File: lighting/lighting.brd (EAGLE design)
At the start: 22.5 x 12.5 mm, 6 parts, among them J1 22-05-3021

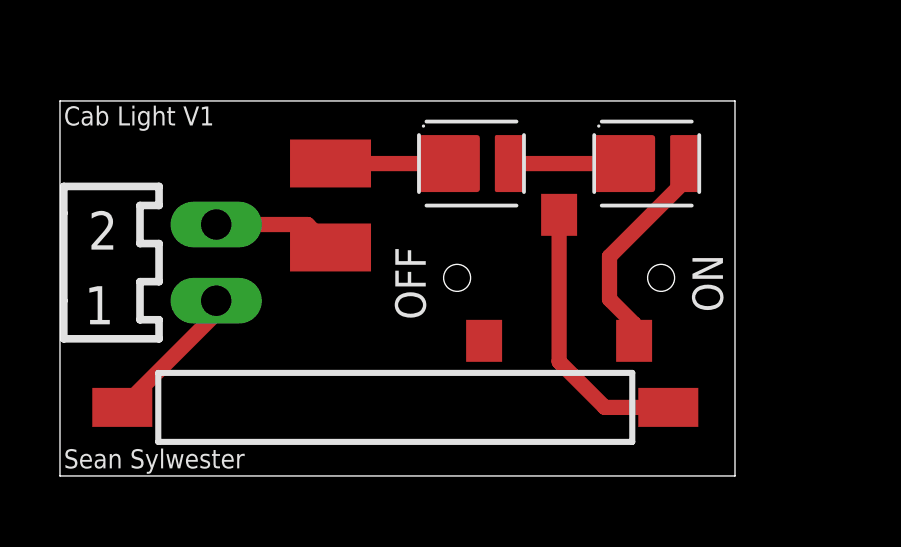
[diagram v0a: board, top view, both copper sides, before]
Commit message: fixed LED direction; GND plane
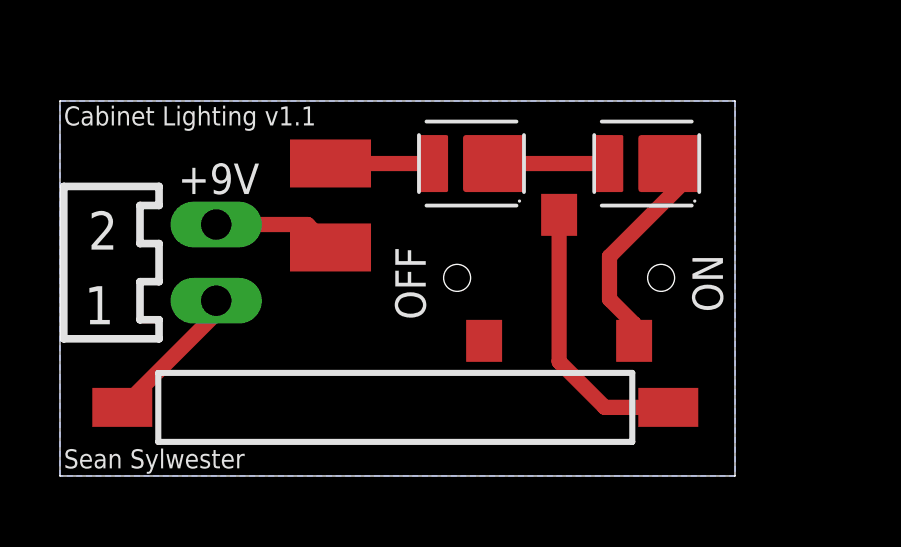
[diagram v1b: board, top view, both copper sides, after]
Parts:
- turned D1 to 180 degrees
- turned D2 to 180 degrees
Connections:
- net N$1 renamed GND
- net N$6 renamed VCC
- net N$3: now also D2.-; no longer D2.+
- net N$4: now also D1.-, D2.+; no longer D1.+, D2.-
- net N$5: now also D1.+; no longer D1.-
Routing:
- net N$5: track 3.97 -> 3.44 mm
- added copper zone on layer 16, net GND
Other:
- board text added: "+9V"
- board text added: "Cabinet Lighting v1.1"
- board text removed: "Cab Light V1"
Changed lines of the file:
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@@
 <setting verticaltext="up"/>
 </settings>
-<grid distance="5" unitdist="mil" unit="mil" style="lines" multiple="1" display="no" altdistance="5" altunitdist="mil" altunit="mil"/>
+<grid distance="1" unitdist="mil" unit="mil" style="lines" multiple="1" display="no" altdistance="5" altunitdist="mil" altunit="mil"/>
 <layers>
 <layer number="1" name="Top" color="4" fill="1" visible="yes" active="yes"/>
@@
 <text x="22.098" y="5.461" size="1.016" layer="21" rot="R90">ON</text>
 <text x="12.192" y="5.207" size="1.016" layer="21" rot="R90">OFF</text>
-<text x="0.127" y="11.684" size="0.635" layer="21">Cab Light V1</text>
+<text x="0.127" y="11.684" size="0.635" layer="21">Cabinet Lighting v1.1</text>
 <text x="0.127" y="0.254" size="0.635" layer="21">Sean Sylwester</text>
+<text x="3.937" y="9.398" size="1.016" layer="21">+9V</text>
 </plain>
 <attributes>
@@
 </class>
 </classes>
-<designrules name="default">
+<designrules name="default *">
 <description language="de">&lt;b&gt;EAGLE Design Rules&lt;/b&gt;
 &lt;p&gt;
@@
 <param name="mdViaViaSameLayer" value="6mil"/>
 <param name="mnLayersViaInSmd" value="2"/>
-<param name="mdCopperDimension" value="40mil"/>
+<param name="mdCopperDimension" value="8mil"/>
 <param name="mdDrill" value="6mil"/>
 <param name="mdSmdStop" value="0mil"/>
@@
 <attribute name="VALUE" x="17.526" y="2.921" size="1.27" layer="27" rot="R180"/>
 </element>
-<element name="D1" library="my_lib" package="LUXEON2835C" value="LUXEON2835C" x="13.716" y="10.414" smashed="yes"/>
-<element name="D2" library="my_lib" package="LUXEON2835C" value="LUXEON2835C" x="19.558" y="10.414" smashed="yes"/>
+<element name="D1" library="my_lib" package="LUXEON2835C" value="LUXEON2835C" x="13.716" y="10.414" smashed="yes" rot="R180"/>
+<element name="D2" library="my_lib" package="LUXEON2835C" value="LUXEON2835C" x="19.558" y="10.414" smashed="yes" rot="R180"/>
 <element name="S2" library="my_lib" package="CL-SB-12B-01T" value="CL-SB-12B-01T" x="16.637" y="6.604" smashed="yes">
 <attribute name="VALUE" x="13.422" y="2.274" size="1.27" layer="27"/>
@@
 </elements>
 <signals>
-<signal name="N$1">
+<signal name="GND">
 <contactref element="S1" pad="2"/>
 <contactref element="J1" pad="1"/>
 <wire x1="2.076" y1="2.286" x2="5.207" y2="5.417" width="0.508" layer="1"/>
 <wire x1="5.207" y1="5.417" x2="5.207" y2="5.842" width="0.508" layer="1"/>
+<polygon width="0.127" layer="16" spacing="0.254" orphans="yes" thermals="no">
+<vertex x="0" y="12.4968"/>
+<vertex x="22.5044" y="12.4968"/>
+<vertex x="22.5044" y="0"/>
+<vertex x="0" y="0"/>
+</polygon>
 </signal>
 <signal name="N$3">
-<contactref element="D2" pad="+"/>
+<contactref element="D2" pad="-"/>
 <contactref element="S2" pad="P$3"/>
 <wire x1="18.317" y1="5.89155" x2="18.317" y2="7.31645" width="0.508" layer="1"/>
 <wire x1="19.137" y1="4.504" x2="19.137" y2="5.07155" width="0.508" layer="1"/>
 <wire x1="19.137" y1="5.07155" x2="18.317" y2="5.89155" width="0.508" layer="1"/>
-<wire x1="20.823" y1="9.82245" x2="20.823" y2="10.414" width="0.508" layer="1"/>
+<wire x1="20.823" y1="9.82245" x2="20.293" y2="10.414" width="0.508" layer="1"/>
 <wire x1="18.317" y1="7.31645" x2="20.823" y2="9.82245" width="0.508" layer="1"/>
 </signal>
 <signal name="N$5">
 <contactref element="R1" pad="2"/>
-<contactref element="D1" pad="-"/>
-<wire x1="12.981" y1="10.414" x2="9.02" y2="10.414" width="0.508" layer="1"/>
+<contactref element="D1" pad="+"/>
+<wire x1="12.451" y1="10.414" x2="9.02" y2="10.414" width="0.508" layer="1"/>
 <wire x1="9.02" y1="10.414" x2="9.017" y2="10.417" width="0.254" layer="1"/>
 </signal>
-<signal name="N$6">
+<signal name="VCC">
 <contactref element="R1" pad="1"/>
 <contactref element="J1" pad="2"/>
@@
 </signal>
 <signal name="N$4">
-<contactref element="D1" pad="+"/>
-<contactref element="D2" pad="-"/>
-<wire x1="14.981" y1="10.414" x2="18.823" y2="10.414" width="0.508" layer="1"/>
+<contactref element="D1" pad="-"/>
+<contactref element="D2" pad="+"/>
+<wire x1="14.451" y1="10.414" x2="18.293" y2="10.414" width="0.508" layer="1"/>
 </signal>
 <signal name="N$2">
@@
 <mfgpreviewcolor name="substratecolor" color="0xFF786E46"/>
 </mfgpreviewcolors>
+<errors>
+</errors>
 </board>
 </drawing>

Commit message: added mounting holes
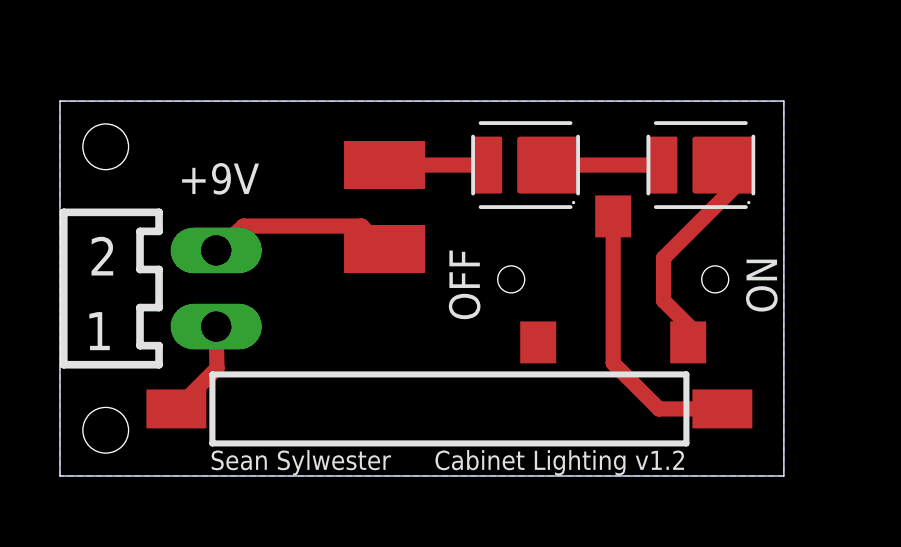
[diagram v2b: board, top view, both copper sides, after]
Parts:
- moved D1 1.80 mm to (15.5, 10.4)
- moved D2 1.80 mm to (21.4, 10.4)
- moved R1 1.80 mm to (10.8, 8.97)
- moved S1 1.80 mm to (13.0, 2.24)
- moved S2 1.80 mm to (18.4, 6.55)
- moved J1 0.86 mm to (5.21, 6.25)
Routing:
- net VCC: track 4.13 -> 6.24 mm
- net GND: track 4.85 -> 3.30 mm
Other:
- board size 22.5 x 12.5 mm -> 24.1 x 12.5 mm
- board text added: "Cabinet Lighting v1.2"
- board text removed: "Cabinet Lighting v1.1"
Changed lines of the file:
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@@
 <layer number="43" name="vRestrict" color="2" fill="10" visible="yes" active="yes"/>
 <layer number="44" name="Drills" color="7" fill="1" visible="no" active="yes"/>
-<layer number="45" name="Holes" color="7" fill="1" visible="no" active="yes"/>
+<layer number="45" name="Holes" color="7" fill="1" visible="yes" active="yes"/>
 <layer number="46" name="Milling" color="3" fill="1" visible="no" active="yes"/>
 <layer number="47" name="Measures" color="7" fill="1" visible="no" active="yes"/>
@@
 <board>
 <plain>
-<wire x1="0" y1="0" x2="22.5" y2="0" width="0" layer="20"/>
-<wire x1="22.5" y1="0" x2="22.5" y2="12.5" width="0" layer="20"/>
-<wire x1="22.5" y1="12.5" x2="0" y2="12.5" width="0" layer="20"/>
-<wire x1="0" y1="12.5" x2="0" y2="0" width="0" layer="20"/>
-<text x="22.098" y="5.461" size="1.016" layer="21" rot="R90">ON</text>
-<text x="12.192" y="5.207" size="1.016" layer="21" rot="R90">OFF</text>
-<text x="0.127" y="11.684" size="0.635" layer="21">Cabinet Lighting v1.1</text>
-<text x="0.127" y="0.254" size="0.635" layer="21">Sean Sylwester</text>
+<wire x1="0" y1="0" x2="24.13" y2="0" width="0" layer="20"/>
+<wire x1="24.13" y1="0" x2="24.13" y2="12.4968" width="0" layer="20"/>
+<wire x1="24.13" y1="12.4968" x2="0" y2="12.4968" width="0" layer="20"/>
+<wire x1="0" y1="12.4968" x2="0" y2="0" width="0" layer="20"/>
+<text x="23.9014" y="5.4102" size="1.016" layer="21" rot="R90">ON</text>
+<text x="13.9954" y="5.1562" size="1.016" layer="21" rot="R90">OFF</text>
+<text x="20.8788" y="0.8382" size="0.635" layer="21" rot="R180">Cabinet Lighting v1.2</text>
+<text x="5.0038" y="0.2032" size="0.635" layer="21">Sean Sylwester</text>
 <text x="3.937" y="9.398" size="1.016" layer="21">+9V</text>
+<hole x="1.524" y="10.9728" drill="1.524"/>
+<hole x="1.524" y="1.524" drill="1.524"/>
 </plain>
 <attributes>
@@
 </autorouter>
 <elements>
-<element name="R1" library="rcl" library_urn="urn:adsk.eagle:library:334" package="R1210" package3d_urn="urn:adsk.eagle:package:23554/2" value="" x="9.017" y="9.017" smashed="yes" rot="R90">
-<attribute name="SPICEPREFIX" value="R" x="29.337" y="36.957" size="1.778" layer="27" rot="R90" display="off"/>
-<attribute name="VALUE" x="12.192" y="6.477" size="1.27" layer="27" rot="R90"/>
+<element name="R1" library="rcl" library_urn="urn:adsk.eagle:library:334" package="R1210" package3d_urn="urn:adsk.eagle:package:23554/2" value="" x="10.8204" y="8.9662" smashed="yes" rot="R90">
+<attribute name="SPICEPREFIX" value="R" x="31.1404" y="36.9062" size="1.778" layer="27" rot="R90" display="off"/>
+<attribute name="VALUE" x="13.9954" y="6.4262" size="1.27" layer="27" rot="R90"/>
 </element>
-<element name="S1" library="switch-reed" library_urn="urn:adsk.eagle:library:379" package="MK15" package3d_urn="urn:adsk.eagle:package:27517/1" value="REED-SWITCH-MK15-B" x="11.176" y="2.286" smashed="yes" rot="R180">
-<attribute name="MF" value="MEDER" x="-16.764" y="31.496" size="1.778" layer="27" rot="R180" display="off"/>
-<attribute name="MPN" value="MK15-B-2" x="-16.764" y="31.496" size="1.778" layer="27" rot="R180" display="off"/>
-<attribute name="OC_FARNELL" value="1079484" x="-16.764" y="31.496" size="1.778" layer="27" rot="R180" display="off"/>
-<attribute name="VALUE" x="17.526" y="2.921" size="1.27" layer="27" rot="R180"/>
+<element name="S1" library="switch-reed" library_urn="urn:adsk.eagle:library:379" package="MK15" package3d_urn="urn:adsk.eagle:package:27517/1" value="REED-SWITCH-MK15-B" x="12.9794" y="2.2352" smashed="yes" rot="R180">
+<attribute name="MF" value="MEDER" x="-14.9606" y="31.4452" size="1.778" layer="27" rot="R180" display="off"/>
+<attribute name="MPN" value="MK15-B-2" x="-14.9606" y="31.4452" size="1.778" layer="27" rot="R180" display="off"/>
+<attribute name="OC_FARNELL" value="1079484" x="-14.9606" y="31.4452" size="1.778" layer="27" rot="R180" display="off"/>
+<attribute name="VALUE" x="19.3294" y="2.8702" size="1.27" layer="27" rot="R180"/>
 </element>
-<element name="D1" library="my_lib" package="LUXEON2835C" value="LUXEON2835C" x="13.716" y="10.414" smashed="yes" rot="R180"/>
-<element name="D2" library="my_lib" package="LUXEON2835C" value="LUXEON2835C" x="19.558" y="10.414" smashed="yes" rot="R180"/>
-<element name="S2" library="my_lib" package="CL-SB-12B-01T" value="CL-SB-12B-01T" x="16.637" y="6.604" smashed="yes">
-<attribute name="VALUE" x="13.422" y="2.274" size="1.27" layer="27"/>
+<element name="D1" library="my_lib" package="LUXEON2835C" value="LUXEON2835C" x="15.5194" y="10.3632" smashed="yes" rot="R180"/>
+<element name="D2" library="my_lib" package="LUXEON2835C" value="LUXEON2835C" x="21.3614" y="10.3632" smashed="yes" rot="R180"/>
+<element name="S2" library="my_lib" package="CL-SB-12B-01T" value="CL-SB-12B-01T" x="18.4404" y="6.5532" smashed="yes">
+<attribute name="VALUE" x="15.2254" y="2.2232" size="1.27" layer="27"/>
 </element>
-<element name="J1" library="my_lib" package="7395-02" value="22-05-3021" x="5.207" y="7.112" smashed="yes" rot="R270">
-<attribute name="VALUE" x="2.7671" y="3.7099" size="0.8128" layer="27" ratio="10" rot="R180"/>
+<element name="J1" library="my_lib" package="7395-02" value="22-05-3021" x="5.207" y="6.2484" smashed="yes" rot="R270">
+<attribute name="VALUE" x="2.7671" y="2.8463" size="0.8128" layer="27" ratio="10" rot="R180"/>
 </element>
 </elements>
@@
 <contactref element="S1" pad="2"/>
 <contactref element="J1" pad="1"/>
-<wire x1="2.076" y1="2.286" x2="5.207" y2="5.417" width="0.508" layer="1"/>
-<wire x1="5.207" y1="5.417" x2="5.207" y2="5.842" width="0.508" layer="1"/>
+<wire x1="3.8794" y1="2.2352" x2="5.2324" y2="3.5882" width="0.508" layer="1"/>
+<wire x1="5.2324" y1="3.5882" x2="5.207" y2="4.9784" width="0.508" layer="1"/>
 <polygon width="0.127" layer="16" spacing="0.254" orphans="yes" thermals="no">
 <vertex x="0" y="12.4968"/>
-<vertex x="22.5044" y="12.4968"/>
-<vertex x="22.5044" y="0"/>
+<vertex x="24.13" y="12.4968"/>
+<vertex x="24.13" y="0"/>
 <vertex x="0" y="0"/>
 </polygon>
@@
 <contactref element="D2" pad="-"/>
 <contactref element="S2" pad="P$3"/>
-<wire x1="18.317" y1="5.89155" x2="18.317" y2="7.31645" width="0.508" layer="1"/>
-<wire x1="19.137" y1="4.504" x2="19.137" y2="5.07155" width="0.508" layer="1"/>
-<wire x1="19.137" y1="5.07155" x2="18.317" y2="5.89155" width="0.508" layer="1"/>
-<wire x1="20.823" y1="9.82245" x2="20.293" y2="10.414" width="0.508" layer="1"/>
-<wire x1="18.317" y1="7.31645" x2="20.823" y2="9.82245" width="0.508" layer="1"/>
+<wire x1="20.1204" y1="5.84075" x2="20.1204" y2="7.26565" width="0.508" layer="1"/>
+<wire x1="20.9404" y1="4.4532" x2="20.9404" y2="5.02075" width="0.508" layer="1"/>
+<wire x1="20.9404" y1="5.02075" x2="20.1204" y2="5.84075" width="0.508" layer="1"/>
+<wire x1="22.6264" y1="9.77165" x2="22.0964" y2="10.3632" width="0.508" layer="1"/>
+<wire x1="20.1204" y1="7.26565" x2="22.6264" y2="9.77165" width="0.508" layer="1"/>
 </signal>
 <signal name="N$5">
 <contactref element="R1" pad="2"/>
 <contactref element="D1" pad="+"/>
-<wire x1="12.451" y1="10.414" x2="9.02" y2="10.414" width="0.508" layer="1"/>
-<wire x1="9.02" y1="10.414" x2="9.017" y2="10.417" width="0.254" layer="1"/>
+<wire x1="14.2544" y1="10.3632" x2="10.8234" y2="10.3632" width="0.508" layer="1"/>
+<wire x1="10.8234" y1="10.3632" x2="10.8204" y2="10.3662" width="0.254" layer="1"/>
 </signal>
 <signal name="VCC">
 <contactref element="R1" pad="1"/>
 <contactref element="J1" pad="2"/>
-<wire x1="5.207" y1="8.382" x2="8.252" y2="8.382" width="0.508" layer="1"/>
-<wire x1="8.252" y1="8.382" x2="9.017" y2="7.617" width="0.508" layer="1"/>
+<wire x1="10.0554" y1="8.3312" x2="6.121290625" y2="8.3312" width="0.508" layer="1"/>
+<wire x1="5.207" y1="7.5184" x2="6.121290625" y2="8.3312" width="0.508" layer="1"/>
+<wire x1="10.0554" y1="8.3312" x2="10.8204" y2="7.5662" width="0.508" layer="1"/>
 </signal>
 <signal name="N$4">
 <contactref element="D1" pad="-"/>
 <contactref element="D2" pad="+"/>
-<wire x1="14.451" y1="10.414" x2="18.293" y2="10.414" width="0.508" layer="1"/>
+<wire x1="16.2544" y1="10.3632" x2="20.0964" y2="10.3632" width="0.508" layer="1"/>
 </signal>
 <signal name="N$2">
 <contactref element="S2" pad="P$2"/>
 <contactref element="S1" pad="1"/>
-<wire x1="20.276" y1="2.286" x2="18.161" y2="2.286" width="0.508" layer="1"/>
-<wire x1="18.161" y1="2.286" x2="16.637" y2="3.81" width="0.508" layer="1"/>
-<wire x1="16.637" y1="3.81" x2="16.637" y2="8.704" width="0.508" layer="1"/>
+<wire x1="22.0794" y1="2.2352" x2="19.9644" y2="2.2352" width="0.508" layer="1"/>
+<wire x1="19.9644" y1="2.2352" x2="18.4404" y2="3.7592" width="0.508" layer="1"/>
+<wire x1="18.4404" y1="3.7592" x2="18.4404" y2="8.6532" width="0.508" layer="1"/>
 </signal>
 </signals>
@@
 <mfgpreviewcolor name="substratecolor" color="0xFF786E46"/>
 </mfgpreviewcolors>
-<errors>
-</errors>
 </board>
 </drawing>

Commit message: added sim; added switch-off timer; updated pcb
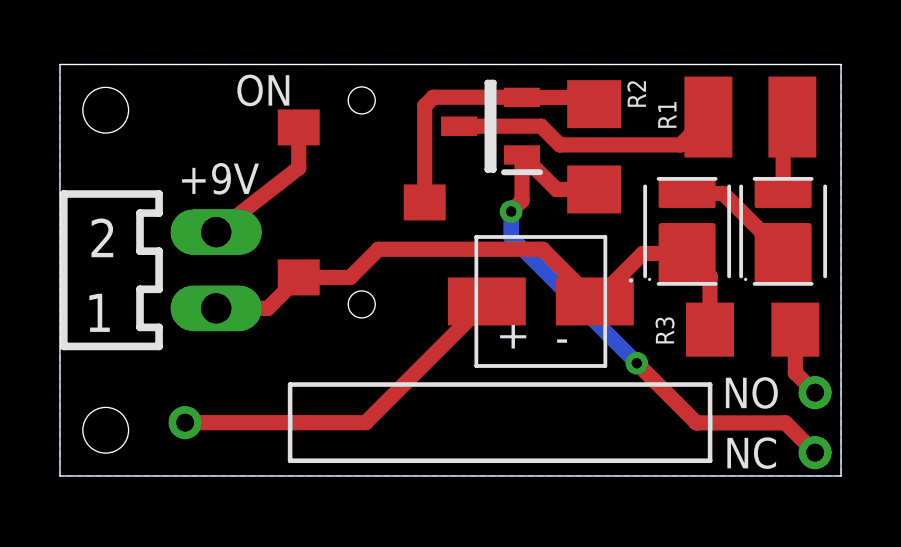
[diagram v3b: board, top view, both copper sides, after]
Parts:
- removed S1: REED-SWITCH-MK15-B, switch-reed:MK15
- added C1: WE-CAP, my_lib:WE-CAP
- added Q1: DMP3099L-7, SamacSys_Parts:SOT96P240X120-3N
- added R2: 2.2M, rcl:R1206
- added R3: 10k, rcl:R1206
- added U$1: KSK-1C90U, my_lib:KSK-1C90U
- moved R1 12.6 mm to (23.0, 12.0), turned to 0 degrees
- moved D1 8.87 mm to (24.1, 8.15), turned to 90 degrees
- moved S2 8.77 mm to (10.1, 9.12), turned to 270 degrees
- moved D2 2.26 mm to (20.9, 8.15), turned to 90 degrees
- moved J1 0.61 mm to (5.21, 6.86)
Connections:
- removed net N$2 (its old number): S1.1, S2.P$2
- new net COM: C1.+, U$1.COM
- new net NC: Q1.1, R2.1, U$1.NC
- new net NO: R3.2, U$1.NO
- new net PWR: Q1.2, R2.2, S2.P$2
- net GND: now also C1.-, D2.-, R3.1, S2.P$3; no longer S1.2
- net N$3: now also Q1.3, R1.1; no longer D2.-, S2.P$3
- net VCC: now also S2.P$1; no longer R1.1
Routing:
- net NC: track 0.00 -> 18.9 mm, vias 0 -> 2
- net GND: track 3.30 -> 20.8 mm
- net COM: track 0.00 -> 11.7 mm
- net N$2 (its old number): track 9.16 -> 0.00 mm
- net PWR: track 0.00 -> 9.08 mm
- net NO: track 0.00 -> 2.37 mm
- net N$3: track 7.49 -> 8.95 mm
- net VCC: track 6.24 -> 4.84 mm
- net N$2: track 3.44 -> 2.67 mm
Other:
- board size 24.1 x 12.5 mm -> 26 x 13.7 mm
- board text added: "+"
- board text added: "-"
- board text added: "Cabinet Lighting v2.0"
- board text added: "NC"
- board text added: "NO"
- board text removed: "Cabinet Lighting v1.2"
- board text removed: "OFF"
